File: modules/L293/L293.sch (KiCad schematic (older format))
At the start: 24 parts, among them J1 2, J10 11, J11 12, J12 13, J13 A0, J14 A1, J15 A2, J16 A3, J17 A4, J18 A5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

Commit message: L293
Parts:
- added U1: L293D, Package_DIP:DIP-16_W7.62mm, symbol Driver_Motor:L293D
- added U? (x4): 74LVC1G79, symbol 74xGxx:74LVC1G79
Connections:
- net GND: now also U?.3 (GND), U?.3 (GND), U?.3 (GND), U?.3 (GND)
- net VCC: now also U?.5 (VCC), U?.5 (VCC), U?.5 (VCC), U?.5 (VCC)
- new net: U1.10 (3A), U?.4 (Q)
- new net: U1.15 (4A), U?.4 (Q)
- new net: U1.2 (1A), U?.4 (Q)
- new net: U1.7 (2A), U?.4 (Q)
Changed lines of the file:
@@
 EESchema Schematic File Version 4
-LIBS:Harduino-cache
+LIBS:L293-cache
 EELAYER 30 0
 EELAYER END
@@
 Connection ~ 6550 3550
 Connection ~ 6550 3700
+$Comp
+L Driver_Motor:L293D U1
+U 1 1 5E4E1F7C
+P 3750 3100
+F 0 "U1" H 3750 4281 50  0000 C CNN
+F 1 "L293D" H 3750 4190 50  0000 C CNN
+F 2 "Package_DIP:DIP-16_W7.62mm" H 4000 2350 50  0001 L CNN
+F 3 "http://www.ti.com/lit/ds/symlink/l293.pdf" H 3450 3800 50  0001 C CNN
+	1    3750 3100
+	1    0    0    -1
+$EndComp
+$Comp
+L 74xGxx:74LVC1G79 U?
+U 1 1 5E4E5DE1
+P 2200 2600
+F 0 "U?" H 2200 2917 50  0000 C CNN
+F 1 "74LVC1G79" H 2200 2826 50  0000 C CNN
+F 2 "" H 2200 2600 50  0001 C CNN
+F 3 "http://www.ti.com/lit/sg/scyt129e/scyt129e.pdf" H 2200 2600 50  0001 C CNN
+	1    2200 2600
+	1    0    0    -1
+$EndComp
+$Comp
+L 74xGxx:74LVC1G79 U?
+U 1 1 5E4E6677
+P 2200 3100
+F 0 "U?" H 2200 3417 50  0000 C CNN
+F 1 "74LVC1G79" H 2200 3326 50  0000 C CNN
+F 2 "" H 2200 3100 50  0001 C CNN
+F 3 "http://www.ti.com/lit/sg/scyt129e/scyt129e.pdf" H 2200 3100 50  0001 C CNN
+	1    2200 3100
+	1    0    0    -1
+$EndComp
+$Comp
+L 74xGxx:74LVC1G79 U?
+U 1 1 5E4E6CD5
+P 2200 3600
+F 0 "U?" H 2200 3917 50  0000 C CNN
+F 1 "74LVC1G79" H 2200 3826 50  0000 C CNN
+F 2 "" H 2200 3600 50  0001 C CNN
+F 3 "http://www.ti.com/lit/sg/scyt129e/scyt129e.pdf" H 2200 3600 50  0001 C CNN
+	1    2200 3600
+	1    0    0    -1
+$EndComp
+$Comp
+L 74xGxx:74LVC1G79 U?
+U 1 1 5E4E7283
+P 2200 4100
+F 0 "U?" H 2200 4417 50  0000 C CNN
+F 1 "74LVC1G79" H 2200 4326 50  0000 C CNN
+F 2 "" H 2200 4100 50  0001 C CNN
+F 3 "http://www.ti.com/lit/sg/scyt129e/scyt129e.pdf" H 2200 4100 50  0001 C CNN
+	1    2200 4100
+	1    0    0    -1
+$EndComp
+Wire Wire Line
+	2450 2500 3250 2500
+Wire Wire Line
+	2450 3000 2575 3000
+Wire Wire Line
+	2575 3000 2575 2700
+Wire Wire Line
+	2575 2700 3250 2700
+Wire Wire Line
+	2450 3500 2750 3500
+Wire Wire Line
+	2750 3500 2750 3100
+Wire Wire Line
+	2750 3100 3250 3100
+Wire Wire Line
+	2450 4000 2950 4000
+Wire Wire Line
+	3250 3300 2950 3300
+Wire Wire Line
+	2950 3300 2950 4000
 $EndSCHEMATC

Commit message: L293 sch
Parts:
- added C1, C2: 0.1uF, Capacitor_SMD:C_0805_2012Metric_Pad1.15x1.40mm_HandSolder, symbol Device:C
- added J21: Pwr, TerminalBlock:TerminalBlock_bornier-2_P5.08mm, symbol Connector:Screw_Terminal_01x02
- added J22: M1, TerminalBlock:TerminalBlock_bornier-2_P5.08mm, symbol Connector:Screw_Terminal_01x02
- added J23: M2, TerminalBlock:TerminalBlock_bornier-2_P5.08mm, symbol Connector:Screw_Terminal_01x02
- U1, U2, U3, U4: renamed from U?; footprint (none) -> Package_TO_SOT_SMD:SOT-23-5_HandSoldering
- renumbered U1 to U5
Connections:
- net GND: now also U5.12 (GND), U5.13 (GND), U5.4 (GND), U5.5 (GND), C1.2, C2.1, J21.2 (Pin_2)
- net VCC: now also U5.16 (VCC1), C1.1
- net at J2.1 (Pin_1): now also U1.2 (C), U2.2 (C), U3.2 (C), U4.2 (C)
- net at J3.1 (Pin_1): now also U1.1 (D)
- net at J4.1 (Pin_1): now also U2.1 (D)
- net at J5.1 (Pin_1): now also U3.1 (D)
- net at J6.1 (Pin_1): now also U4.1 (D)
- net at J9.1 (Pin_1): now also U5.1 (EN1,2)
- net at J10.1 (Pin_1): now also U5.9 (EN3,4)
- net at U5.11 (3Y): now also J23.1 (Pin_1)
- net at U5.14 (4Y): now also J23.2 (Pin_2)
- net at U5.3 (1Y): now also J22.1 (Pin_1)
- net at U5.6 (2Y): now also J22.2 (Pin_2)
- net at U5.8 (VCC2): now also C2.2, J21.1 (Pin_1)
- no-connect marks 0 -> 11
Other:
- moved on the sheet: U1, U2, U3, U4, U5

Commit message: L293 pcb ready
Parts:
- added C3: 0.1uF, Capacitor_SMD:C_0805_2012Metric_Pad1.15x1.40mm_HandSolder, symbol Device:C
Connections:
- net GND: now also C3.2
- net VCC: now also C3.1
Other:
- moved on the sheet: C1
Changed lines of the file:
@@
 L power:VCC #PWR01002
 U 1 1 5E4FBE8D
-P 3600 2125
-F 0 "#PWR01002" H 3600 1975 50  0001 C CNN
-F 1 "VCC" H 3617 2298 50  0000 C CNN
-F 2 "" H 3600 2125 50  0001 C CNN
-F 3 "" H 3600 2125 50  0001 C CNN
-	1    3600 2125
+P 3600 1625
+F 0 "#PWR01002" H 3600 1475 50  0001 C CNN
+F 1 "VCC" H 3617 1798 50  0000 C CNN
+F 2 "" H 3600 1625 50  0001 C CNN
+F 3 "" H 3600 1625 50  0001 C CNN
+	1    3600 1625
 	1    0    0    -1
 $EndComp
 Wire Wire Line
-	3600 2125 3600 2250
+	3600 1625 3600 1750
 $Comp
 L Device:C C1
 U 1 1 5E4FDA62
-P 3275 2250
-F 0 "C1" V 3023 2250 50  0000 C CNN
-F 1 "0.1uF" V 3114 2250 50  0000 C CNN
-F 2 "Capacitor_SMD:C_0805_2012Metric_Pad1.15x1.40mm_HandSolder" H 3313 2100 50  0001 C CNN
-F 3 "~" H 3275 2250 50  0001 C CNN
-	1    3275 2250
+P 3275 1750
+F 0 "C1" V 3225 1650 50  0000 C CNN
+F 1 "0.1uF" V 3225 1900 50  0000 C CNN
+F 2 "Capacitor_SMD:C_0805_2012Metric_Pad1.15x1.40mm_HandSolder" H 3313 1600 50  0001 C CNN
+F 3 "~" H 3275 1750 50  0001 C CNN
+	1    3275 1750
 	0    1    1    0
 $EndComp
@@
 L power:GND #PWR01001
 U 1 1 5E4FF1E7
-P 3050 2250
-F 0 "#PWR01001" H 3050 2000 50  0001 C CNN
-F 1 "GND" V 3055 2122 50  0000 R CNN
-F 2 "" H 3050 2250 50  0001 C CNN
-F 3 "" H 3050 2250 50  0001 C CNN
-	1    3050 2250
+P 3050 1750
+F 0 "#PWR01001" H 3050 1500 50  0001 C CNN
+F 1 "GND" V 3055 1622 50  0000 R CNN
+F 2 "" H 3050 1750 50  0001 C CNN
+F 3 "" H 3050 1750 50  0001 C CNN
+	1    3050 1750
 	0    1    1    0
 $EndComp
 Wire Wire Line
-	3050 2250 3125 2250
+	3050 1750 3125 1750
 Wire Wire Line
-	3425 2250 3600 2250
-Connection ~ 3600 2250
-Wire Wire Line
-	3600 2250 3600 2400
+	3425 1750 3600 1750
+Connection ~ 3600 1750
 $Comp
 L Connector:Screw_Terminal_01x02 J21
@@
 NoConn ~ 6750 3100
 NoConn ~ 6750 3250
+$Comp
+L Device:C C3
+U 1 1 5E4FFB73
+P 3275 2050
+F 0 "C3" V 3225 1950 50  0000 C CNN
+F 1 "0.1uF" V 3225 2200 50  0000 C CNN
+F 2 "Capacitor_SMD:C_0805_2012Metric_Pad1.15x1.40mm_HandSolder" H 3313 1900 50  0001 C CNN
+F 3 "~" H 3275 2050 50  0001 C CNN
+	1    3275 2050
+	0    1    1    0
+$EndComp
+$Comp
+L power:GND #PWR01
+U 1 1 5E4FFF70
+P 3050 2050
+F 0 "#PWR01" H 3050 1800 50  0001 C CNN
+F 1 "GND" V 3055 1922 50  0000 R CNN
+F 2 "" H 3050 2050 50  0001 C CNN
+F 3 "" H 3050 2050 50  0001 C CNN
+	1    3050 2050
+	0    1    1    0
+$EndComp
+Wire Wire Line
+	3125 2050 3050 2050
+Wire Wire Line
+	3600 1750 3600 2050
+Wire Wire Line
+	3425 2050 3600 2050
+Connection ~ 3600 2050
+Wire Wire Line
+	3600 2050 3600 2400
 $EndSCHEMATC

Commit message: Add pull-up and cap
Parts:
- added C4: 500uF, Capacitor_THT:CP_Radial_D8.0mm_P3.50mm, symbol Device:CP
- added R1: 10k, Resistor_SMD:R_0805_2012Metric_Pad1.15x1.40mm_HandSolder, symbol Device:R
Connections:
- net GND: now also C4.2, R1.1
- net at J2.1 (Pin_1), U1.2 (C), U2.2 (C)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: now also R1.2
- net at C2.2, J21.1 (Pin_1), U5.8 (VCC2): now also C4.1
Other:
- moved on the sheet: C2, J21
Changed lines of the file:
@@
 L Connector:Screw_Terminal_01x02 J21
 U 1 1 5E5027C6
-P 4575 2075
-F 0 "J21" H 4655 2067 50  0000 L CNN
-F 1 "Pwr" H 4655 1976 50  0000 L CNN
-F 2 "TerminalBlock:TerminalBlock_bornier-2_P5.08mm" H 4575 2075 50  0001 C CNN
-F 3 "~" H 4575 2075 50  0001 C CNN
-	1    4575 2075
+P 4575 1800
+F 0 "J21" H 4655 1792 50  0000 L CNN
+F 1 "Pwr" H 4655 1701 50  0000 L CNN
+F 2 "TerminalBlock:TerminalBlock_bornier-2_P5.08mm" H 4575 1800 50  0001 C CNN
+F 3 "~" H 4575 1800 50  0001 C CNN
+	1    4575 1800
 	1    0    0    -1
 $EndComp
@@
 L power:GND #PWR01004
 U 1 1 5E51472C
-P 4275 2375
-F 0 "#PWR01004" H 4275 2125 50  0001 C CNN
-F 1 "GND" H 4280 2202 50  0000 C CNN
-F 2 "" H 4275 2375 50  0001 C CNN
-F 3 "" H 4275 2375 50  0001 C CNN
-	1    4275 2375
+P 4275 2100
+F 0 "#PWR01004" H 4275 1850 50  0001 C CNN
+F 1 "GND" H 4280 1927 50  0000 C CNN
+F 2 "" H 4275 2100 50  0001 C CNN
+F 3 "" H 4275 2100 50  0001 C CNN
+	1    4275 2100
 	1    0    0    -1
 $EndComp
 Wire Wire Line
-	3800 2400 3800 2075
-Wire Wire Line
-	3800 2075 4175 2075
+	3800 1800 3950 1800
 $Comp
 L Device:C C2
 U 1 1 5E518FB6
-P 4175 2225
-F 0 "C2" H 4150 2125 50  0000 R CNN
-F 1 "0.1uF" H 4150 2325 50  0000 R CNN
-F 2 "Capacitor_SMD:C_0805_2012Metric_Pad1.15x1.40mm_HandSolder" H 4213 2075 50  0001 C CNN
-F 3 "~" H 4175 2225 50  0001 C CNN
-	1    4175 2225
+P 4175 1950
+F 0 "C2" H 4150 1850 50  0000 R CNN
+F 1 "0.1uF" H 4150 2050 50  0000 R CNN
+F 2 "Capacitor_SMD:C_0805_2012Metric_Pad1.15x1.40mm_HandSolder" H 4213 1800 50  0001 C CNN
+F 3 "~" H 4175 1950 50  0001 C CNN
+	1    4175 1950
 	-1   0    0    1
 $EndComp
-Connection ~ 4175 2075
+Connection ~ 4175 1800
 Wire Wire Line
-	4175 2075 4375 2075
+	4175 1800 4375 1800
 Wire Wire Line
-	4175 2375 4275 2375
+	4175 2100 4275 2100
 Wire Wire Line
-	4375 2375 4275 2375
+	4375 2100 4275 2100
 Wire Wire Line
-	4375 2175 4375 2375
-Connection ~ 4275 2375
+	4375 1900 4375 2100
+Connection ~ 4275 2100
 $Comp
 L power:PWR_FLAG #FLG0103
 U 1 1 5E5201BC
-P 4175 2075
-F 0 "#FLG0103" H 4175 2150 50  0001 C CNN
-F 1 "PWR_FLAG" H 4175 2248 50  0000 C CNN
-F 2 "" H 4175 2075 50  0001 C CNN
-F 3 "~" H 4175 2075 50  0001 C CNN
-	1    4175 2075
+P 4175 1800
+F 0 "#FLG0103" H 4175 1875 50  0001 C CNN
+F 1 "PWR_FLAG" H 4175 1973 50  0000 C CNN
+F 2 "" H 4175 1800 50  0001 C CNN
+F 3 "~" H 4175 1800 50  0001 C CNN
+	1    4175 1800
 	1    0    0    -1
 $EndComp
@@
 Wire Wire Line
 	3600 2050 3600 2400
+$Comp
+L Device:R R1
+U 1 1 5E5CB29D
+P 1750 2400
+F 0 "R1" H 1820 2446 50  0000 L CNN
+F 1 "10k" H 1820 2355 50  0000 L CNN
+F 2 "Resistor_SMD:R_0805_2012Metric_Pad1.15x1.40mm_HandSolder" V 1680 2400 50  0001 C CNN
+F 3 "~" H 1750 2400 50  0001 C CNN
+	1    1750 2400
+	1    0    0    -1
+$EndComp
+$Comp
+L power:GND #PWR02
+U 1 1 5E5CBCE8
+P 1750 2100
+F 0 "#PWR02" H 1750 1850 50  0001 C CNN
+F 1 "GND" H 1755 1927 50  0000 C CNN
+F 2 "" H 1750 2100 50  0001 C CNN
+F 3 "" H 1750 2100 50  0001 C CNN
+	1    1750 2100
+	-1   0    0    1
+$EndComp
+Wire Wire Line
+	1750 2100 1750 2250
+Wire Wire Line
+	1750 2550 1750 2650
+Connection ~ 1750 2650
+Wire Wire Line
+	3800 1800 3800 2400
+$Comp
+L Device:CP C4
+U 1 1 5E5DD515
+P 3950 1950
+F 0 "C4" H 3975 2050 50  0000 L CNN
+F 1 "500uF" H 3950 1850 50  0000 L CNN
+F 2 "Capacitor_THT:CP_Radial_D8.0mm_P3.50mm" H 3988 1800 50  0001 C CNN
+F 3 "~" H 3950 1950 50  0001 C CNN
+	1    3950 1950
+	1    0    0    -1
+$EndComp
+Connection ~ 3950 1800
+Wire Wire Line
+	3950 1800 4175 1800
+$Comp
+L power:GND #PWR03
+U 1 1 5E5DE68D
+P 3950 2100
+F 0 "#PWR03" H 3950 1850 50  0001 C CNN
+F 1 "GND" H 3955 1927 50  0000 C CNN
+F 2 "" H 3950 2100 50  0001 C CNN
+F 3 "" H 3950 2100 50  0001 C CNN
+	1    3950 2100
+	1    0    0    -1
+$EndComp
 $EndSCHEMATC

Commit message: Replace SOT23-5 to TSSOP5
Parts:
- U1, U2, U3, U4: footprint Package_TO_SOT_SMD:SOT-23-5_HandSoldering -> CommonLibrary:tssop5
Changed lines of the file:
@@
 F 0 "U1" H 2150 3217 50  0000 C CNN
 F 1 "74LVC1G79" H 2150 3126 50  0000 C CNN
-F 2 "Package_TO_SOT_SMD:SOT-23-5_HandSoldering" H 2150 2900 50  0001 C CNN
+F 2 "CommonLibrary:tssop5" H 2150 2900 50  0001 C CNN
 F 3 "http://www.ti.com/lit/sg/scyt129e/scyt129e.pdf" H 2150 2900 50  0001 C CNN
 	1    2150 2900
@@
 F 0 "U2" H 2150 3717 50  0000 C CNN
 F 1 "74LVC1G79" H 2150 3626 50  0000 C CNN
-F 2 "Package_TO_SOT_SMD:SOT-23-5_HandSoldering" H 2150 3400 50  0001 C CNN
+F 2 "CommonLibrary:tssop5" H 2150 3400 50  0001 C CNN
 F 3 "http://www.ti.com/lit/sg/scyt129e/scyt129e.pdf" H 2150 3400 50  0001 C CNN
 	1    2150 3400
@@
 F 0 "U3" H 2150 4217 50  0000 C CNN
 F 1 "74LVC1G79" H 2150 4126 50  0000 C CNN
-F 2 "Package_TO_SOT_SMD:SOT-23-5_HandSoldering" H 2150 3900 50  0001 C CNN
+F 2 "CommonLibrary:tssop5" H 2150 3900 50  0001 C CNN
 F 3 "http://www.ti.com/lit/sg/scyt129e/scyt129e.pdf" H 2150 3900 50  0001 C CNN
 	1    2150 3900
@@
 F 0 "U4" H 2150 4717 50  0000 C CNN
 F 1 "74LVC1G79" H 2150 4626 50  0000 C CNN
-F 2 "Package_TO_SOT_SMD:SOT-23-5_HandSoldering" H 2150 4400 50  0001 C CNN
+F 2 "CommonLibrary:tssop5" H 2150 4400 50  0001 C CNN
 F 3 "http://www.ti.com/lit/sg/scyt129e/scyt129e.pdf" H 2150 4400 50  0001 C CNN
 	1    2150 4400

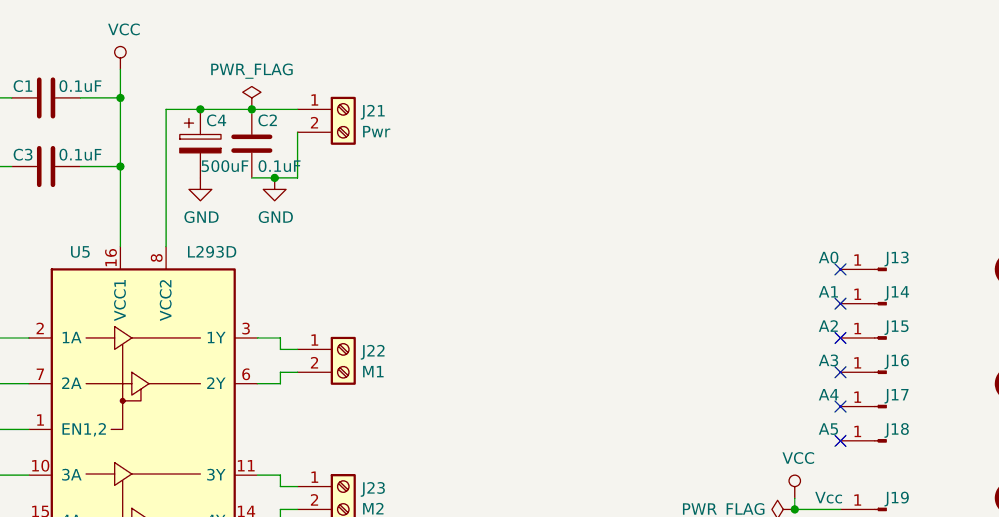
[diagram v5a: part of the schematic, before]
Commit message: Add L4940 to motor shield
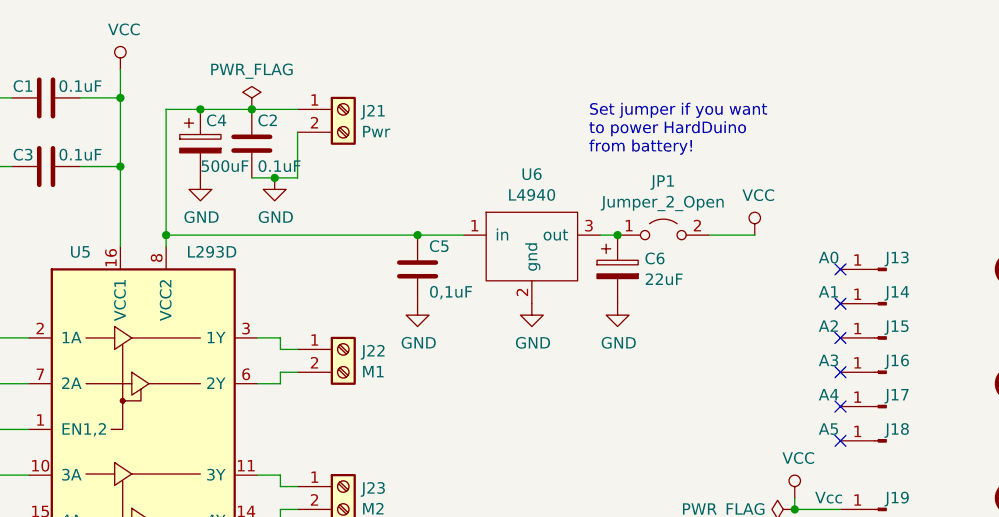
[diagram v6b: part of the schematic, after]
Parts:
- added C5: 0,1uF, Capacitor_SMD:C_0805_2012Metric_Pad1.15x1.40mm_HandSolder, symbol Device:C
- added C6: 22uF, Capacitor_THT:CP_Radial_D5.0mm_P2.50mm, symbol Device:CP
- added JP1: Jumper_2_Open, Connector_PinHeader_2.54mm:PinHeader_1x02_P2.54mm_Vertical, symbol Jumper:Jumper_2_Open
- added U6: L4940, Package_TO_SOT_THT:TO-220-3_Vertical, symbol CommonLibrary:L4940
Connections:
- net GND: now also C5.2, C6.2, U6.2 (gnd)
- net VCC: now also JP1.2 (B)
- net at C2.2, C4.1, J21.1 (Pin_1)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: now also C5.1, U6.1 (in)
- new net: C6.1, JP1.1 (A), U6.3 (out)
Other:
- note added: "Set jumper if you want\nto power HardDuino\nfrom battery!"
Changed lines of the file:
@@
 Connection ~ 1750 2650
 Wire Wire Line
-	3800 1800 3800 2400
+	3800 1800 3800 2350
 $Comp
 L Device:CP C4
@@
 	1    0    0    -1
 $EndComp
+$Comp
+L CommonLibrary:L4940 U6
+U 1 1 5E6BBCDA
+P 5400 2250
+F 0 "U6" H 5400 2415 50  0000 C CNN
+F 1 "L4940" H 5400 2324 50  0000 C CNN
+F 2 "Package_TO_SOT_THT:TO-220-3_Vertical" H 5250 2300 50  0001 C CNN
+F 3 "" H 5250 2300 50  0001 C CNN
+	1    5400 2250
+	1    0    0    -1
+$EndComp
+$Comp
+L power:GND #PWR05
+U 1 1 5E6C2000
+P 5400 2650
+F 0 "#PWR05" H 5400 2400 50  0001 C CNN
+F 1 "GND" H 5405 2477 50  0000 C CNN
+F 2 "" H 5400 2650 50  0001 C CNN
+F 3 "" H 5400 2650 50  0001 C CNN
+	1    5400 2650
+	1    0    0    -1
+$EndComp
+Wire Wire Line
+	3800 2350 4900 2350
+Connection ~ 3800 2350
+Wire Wire Line
+	3800 2350 3800 2400
+$Comp
+L Device:C C5
+U 1 1 5E6C83B5
+P 4900 2500
+F 0 "C5" H 4950 2600 50  0000 L CNN
+F 1 "0,1uF" H 4950 2400 50  0000 L CNN
+F 2 "Capacitor_SMD:C_0805_2012Metric_Pad1.15x1.40mm_HandSolder" H 4938 2350 50  0001 C CNN
+F 3 "~" H 4900 2500 50  0001 C CNN
+	1    4900 2500
+	1    0    0    -1
+$EndComp
+Connection ~ 4900 2350
+Wire Wire Line
+	4900 2350 5100 2350
+$Comp
+L power:GND #PWR04
+U 1 1 5E6C8A38
+P 4900 2650
+F 0 "#PWR04" H 4900 2400 50  0001 C CNN
+F 1 "GND" H 4905 2477 50  0000 C CNN
+F 2 "" H 4900 2650 50  0001 C CNN
+F 3 "" H 4900 2650 50  0001 C CNN
+	1    4900 2650
+	1    0    0    -1
+$EndComp
+$Comp
+L Device:CP C6
+U 1 1 5E6CA1A7
+P 5775 2500
+F 0 "C6" H 5893 2546 50  0000 L CNN
+F 1 "22uF" H 5893 2455 50  0000 L CNN
+F 2 "Capacitor_THT:CP_Radial_D5.0mm_P2.50mm" H 5813 2350 50  0001 C CNN
+F 3 "~" H 5775 2500 50  0001 C CNN
+	1    5775 2500
+	1    0    0    -1
+$EndComp
+$Comp
+L power:GND #PWR06
+U 1 1 5E6CAAB6
+P 5775 2650
+F 0 "#PWR06" H 5775 2400 50  0001 C CNN
+F 1 "GND" H 5780 2477 50  0000 C CNN
+F 2 "" H 5775 2650 50  0001 C CNN
+F 3 "" H 5775 2650 50  0001 C CNN
+	1    5775 2650
+	1    0    0    -1
+$EndComp
+Wire Wire Line
+	5700 2350 5775 2350
+$Comp
+L Jumper:Jumper_2_Open JP1
+U 1 1 5E6CD8DC
+P 5975 2350
+F 0 "JP1" H 5975 2585 50  0000 C CNN
+F 1 "Jumper_2_Open" H 5975 2494 50  0000 C CNN
+F 2 "Connector_PinHeader_2.54mm:PinHeader_1x02_P2.54mm_Vertical" H 5975 2350 50  0001 C CNN
+F 3 "~" H 5975 2350 50  0001 C CNN
+	1    5975 2350
+	1    0    0    -1
+$EndComp
+Connection ~ 5775 2350
+$Comp
+L power:VCC #PWR07
+U 1 1 5E6CE5E9
+P 6375 2350
+F 0 "#PWR07" H 6375 2200 50  0001 C CNN
+F 1 "VCC" H 6392 2523 50  0000 C CNN
+F 2 "" H 6375 2350 50  0001 C CNN
+F 3 "" H 6375 2350 50  0001 C CNN
+	1    6375 2350
+	1    0    0    -1
+$EndComp
+Wire Wire Line
+	6175 2350 6375 2350
+Text Notes 5650 2000 0    50   ~ 0
+Set jumper if you want\nto power HardDuino\nfrom battery!
 $EndSCHEMATC

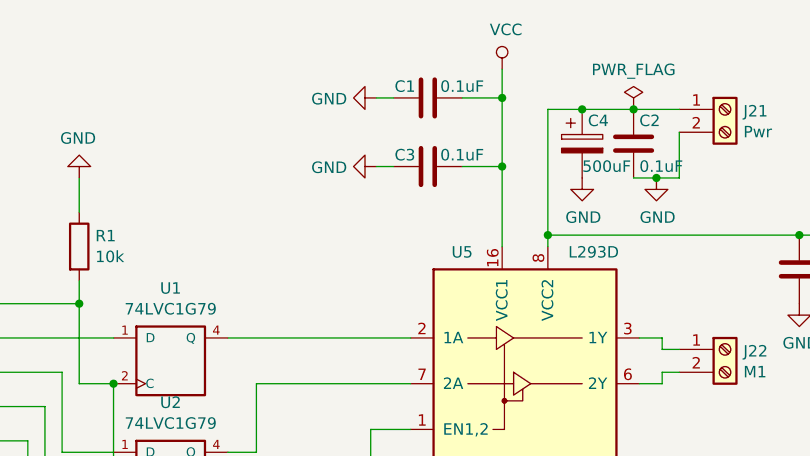
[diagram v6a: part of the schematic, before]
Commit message: Add stab to motor shield
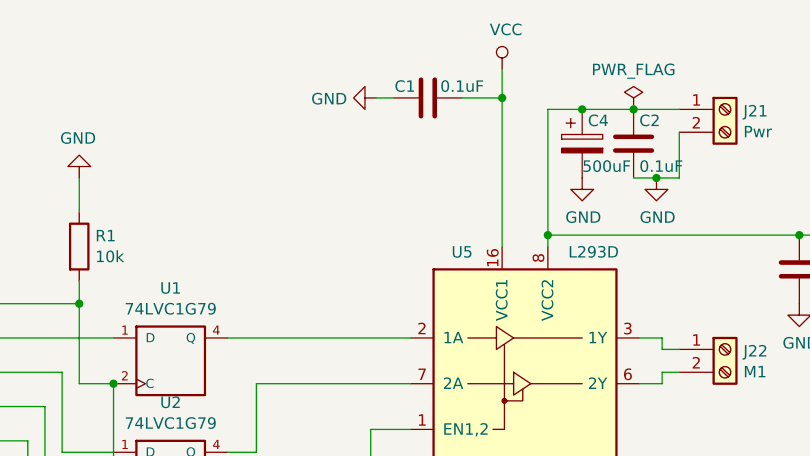
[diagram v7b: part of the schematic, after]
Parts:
- removed C3: 0.1uF, Capacitor_SMD:C_0805_2012Metric_Pad1.15x1.40mm_HandSolder, symbol Device:C
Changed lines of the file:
@@
 NoConn ~ 6750 3250
-$Comp
-L Device:C C3
-U 1 1 5E4FFB73
-P 3275 2050
-F 0 "C3" V 3225 1950 50  0000 C CNN
-F 1 "0.1uF" V 3225 2200 50  0000 C CNN
-F 2 "Capacitor_SMD:C_0805_2012Metric_Pad1.15x1.40mm_HandSolder" H 3313 1900 50  0001 C CNN
-F 3 "~" H 3275 2050 50  0001 C CNN
-	1    3275 2050
-	0    1    1    0
-$EndComp
-$Comp
-L power:GND #PWR01
-U 1 1 5E4FFF70
-P 3050 2050
-F 0 "#PWR01" H 3050 1800 50  0001 C CNN
-F 1 "GND" V 3055 1922 50  0000 R CNN
-F 2 "" H 3050 2050 50  0001 C CNN
-F 3 "" H 3050 2050 50  0001 C CNN
-	1    3050 2050
-	0    1    1    0
-$EndComp
-Wire Wire Line
-	3125 2050 3050 2050
-Wire Wire Line
-	3600 1750 3600 2050
-Wire Wire Line
-	3425 2050 3600 2050
-Connection ~ 3600 2050
-Wire Wire Line
-	3600 2050 3600 2400
 $Comp
 L Device:R R1
@@
 Text Notes 5650 2000 0    50   ~ 0
 Set jumper if you want\nto power HardDuino\nfrom battery!
+Wire Wire Line
+	3600 1750 3600 2400
 $EndSCHEMATC
